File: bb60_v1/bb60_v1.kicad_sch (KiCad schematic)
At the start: 141 parts, among them J1 Conn_01x04, SW1 SW_Push, SW2 SW_Push, U1 STM32F072CBTx, U2 XC6206PxxxMR, U3 USBLC6-2SC6

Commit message: minor changes
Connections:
- net COL1: now also U1.12 (PA2); no longer U1.43 (PB7)
- net COL2: now also U1.11 (PA1); no longer U1.14 (PA4)
- net COL3: now also U1.10 (PA0); no longer U1.13 (PA3)
- net COL4: now also U1.43 (PB7); no longer U1.12 (PA2)
- net COL5: now also U1.14 (PA4); no longer U1.11 (PA1)
- net COL6: now also U1.13 (PA3); no longer U1.10 (PA0)
- net ROW2: now also U1.18 (PB0); no longer U1.16 (PA6)
- net ROW4: now also U1.16 (PA6); no longer U1.18 (PB0)
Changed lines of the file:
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@@
 	)
 	(label "ROW2"
-		(at 60.96 52.07 0)
-		(effects
-			(font
-				(size 1.27 1.27)
-			)
-			(justify left bottom)
+		(at 25.4 64.77 180)
+		(effects
+			(font
+				(size 1.27 1.27)
+			)
+			(justify right bottom)
 		)
 	)
 	(label "COL1"
-		(at 25.4 82.55 180)
-		(effects
-			(font
-				(size 1.27 1.27)
-			)
-			(justify right bottom)
+		(at 60.96 41.91 0)
+		(effects
+			(font
+				(size 1.27 1.27)
+			)
+			(justify left bottom)
 		)
 	)
@@
 	)
 	(label "COL6"
-		(at 60.96 36.83 0)
+		(at 60.96 44.45 0)
 		(effects
 			(font
@@
 	)
 	(label "COL2"
-		(at 60.96 46.99 0)
+		(at 60.96 39.37 0)
 		(effects
 			(font
@@
 	)
 	(label "COL3"
-		(at 60.96 44.45 0)
+		(at 60.96 36.83 0)
 		(effects
 			(font
@@
 	)
 	(label "COL5"
-		(at 60.96 39.37 0)
+		(at 60.96 46.99 0)
 		(effects
 			(font
@@
 	)
 	(label "COL4"
-		(at 60.96 41.91 0)
-		(effects
-			(font
-				(size 1.27 1.27)
-			)
-			(justify left bottom)
+		(at 25.4 82.55 180)
+		(effects
+			(font
+				(size 1.27 1.27)
+			)
+			(justify right bottom)
 		)
 	)
 	(label "ROW4"
-		(at 25.4 64.77 180)
-		(effects
-			(font
-				(size 1.27 1.27)
-			)
-			(justify right bottom)
-		)
-	)
+		(at 60.96 52.07 0)
+		(effects
+			(font
+				(size 1.27 1.27)
+			)
+			(justify left bottom)
+		)
+	)

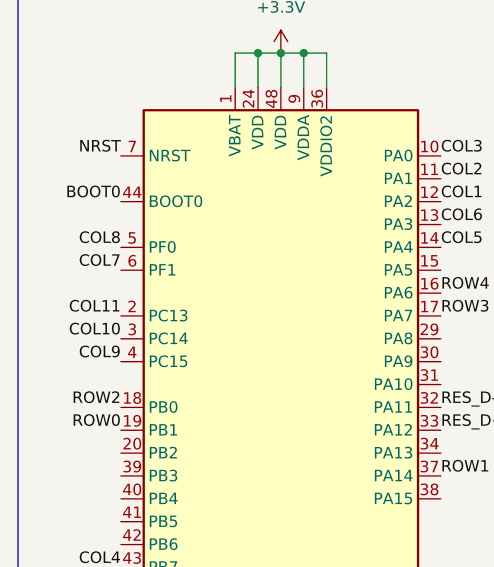
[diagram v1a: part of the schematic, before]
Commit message: Routed traces columns 7-11
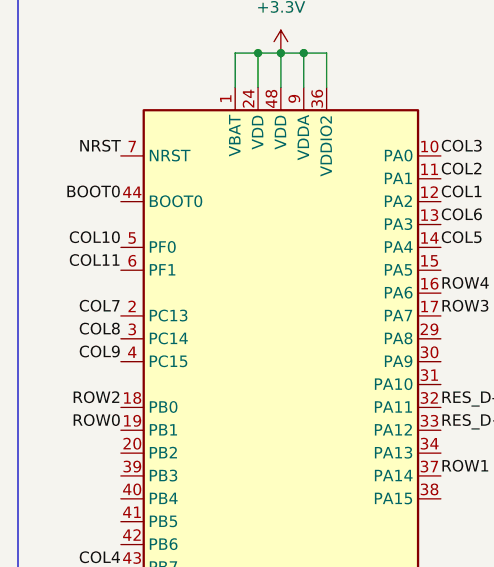
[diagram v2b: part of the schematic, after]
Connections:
- net COL10: now also U1.5 (PF0); no longer U1.3 (PC14)
- net COL11: now also U1.6 (PF1); no longer U1.2 (PC13)
- net COL7: now also U1.2 (PC13); no longer U1.6 (PF1)
- net COL8: now also U1.3 (PC14); no longer U1.5 (PF0)
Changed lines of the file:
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@@
 	)
 	(label "COL11"
-		(at 25.4 54.61 180)
+		(at 25.4 49.53 180)
 		(effects
 			(font
@@
 	)
 	(label "COL8"
-		(at 25.4 46.99 180)
+		(at 25.4 57.15 180)
 		(effects
 			(font
@@
 	)
 	(label "COL7"
-		(at 25.4 49.53 180)
+		(at 25.4 54.61 180)
 		(effects
 			(font
@@
 	)
 	(label "COL10"
-		(at 25.4 57.15 180)
+		(at 25.4 46.99 180)
 		(effects
 			(font

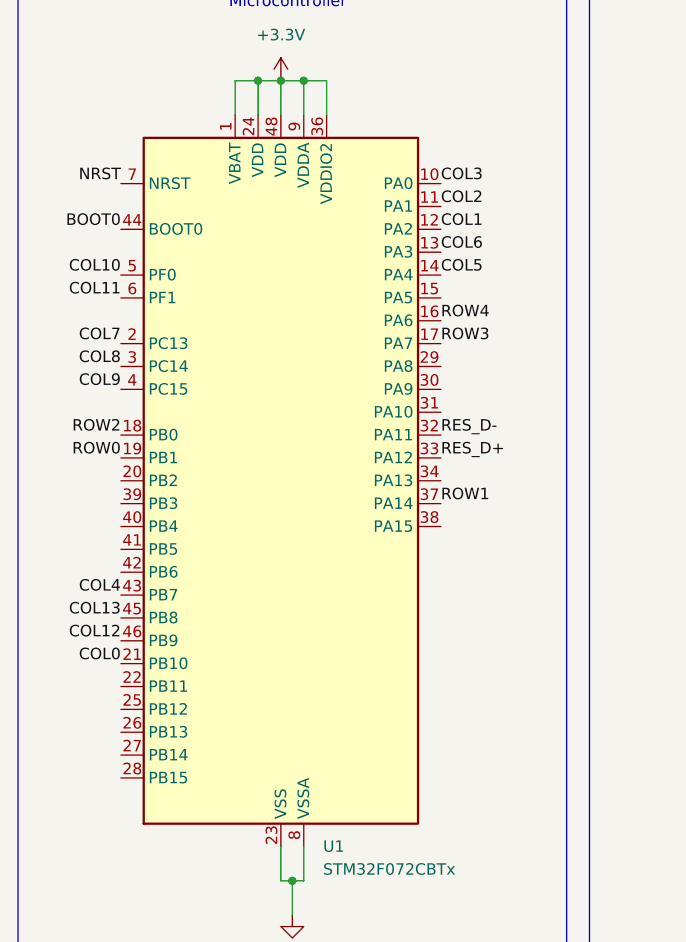
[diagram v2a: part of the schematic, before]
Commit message: finished row/column traces
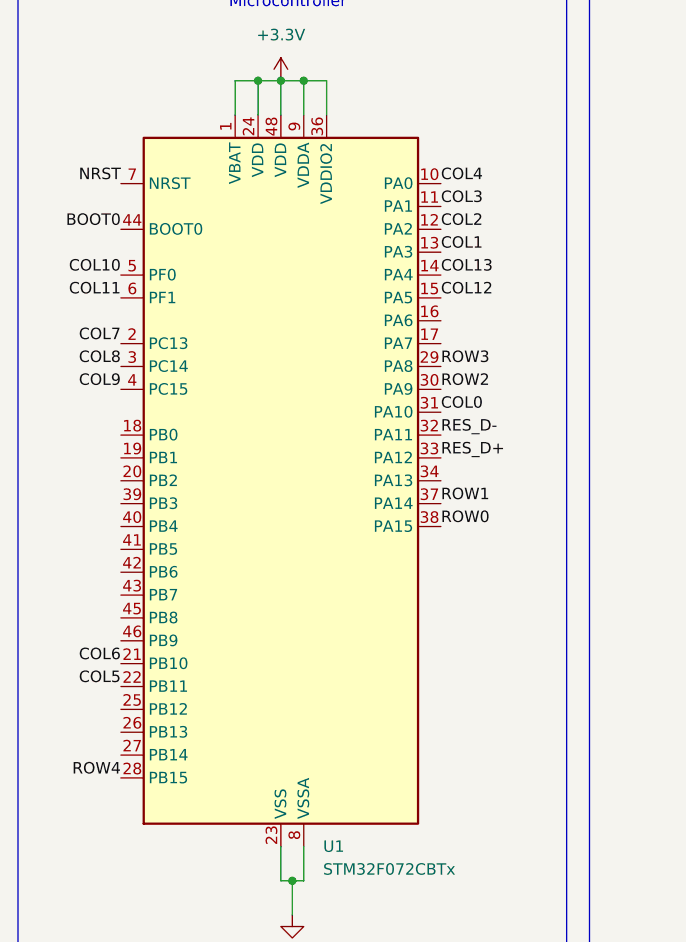
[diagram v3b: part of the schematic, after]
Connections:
- net COL0: now also U1.31 (PA10); no longer U1.21 (PB10)
- net COL1: now also U1.13 (PA3); no longer U1.12 (PA2)
- net COL12: now also U1.15 (PA5); no longer U1.46 (PB9)
- net COL13: now also U1.14 (PA4); no longer U1.45 (PB8)
- net COL2: now also U1.12 (PA2); no longer U1.11 (PA1)
- net COL3: now also U1.11 (PA1); no longer U1.10 (PA0)
- net COL4: now also U1.10 (PA0); no longer U1.43 (PB7)
- net COL5: now also U1.22 (PB11); no longer U1.14 (PA4)
- net COL6: now also U1.21 (PB10); no longer U1.13 (PA3)
- net ROW0: now also U1.38 (PA15); no longer U1.19 (PB1)
- net ROW2: now also U1.30 (PA9); no longer U1.18 (PB0)
- net ROW3: now also U1.29 (PA8); no longer U1.17 (PA7)
- net ROW4: now also U1.28 (PB15); no longer U1.16 (PA6)
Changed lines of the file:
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@@
 	)
 	(label "ROW2"
-		(at 25.4 64.77 180)
-		(effects
-			(font
-				(size 1.27 1.27)
-			)
-			(justify right bottom)
+		(at 60.96 59.69 0)
+		(effects
+			(font
+				(size 1.27 1.27)
+			)
+			(justify left bottom)
 		)
 	)
 	(label "COL1"
-		(at 60.96 41.91 0)
+		(at 60.96 44.45 0)
 		(effects
 			(font
@@
 	)
 	(label "COL0"
+		(at 60.96 62.23 0)
+		(effects
+			(font
+				(size 1.27 1.27)
+			)
+			(justify left bottom)
+		)
+	)
+	(label "COL13"
+		(at 60.96 46.99 0)
+		(effects
+			(font
+				(size 1.27 1.27)
+			)
+			(justify left bottom)
+		)
+	)
+	(label "COL6"
 		(at 25.4 90.17 180)
 		(effects
@@
 			)
 			(justify right bottom)
-		)
-	)
-	(label "COL13"
-		(at 25.4 85.09 180)
-		(effects
-			(font
-				(size 1.27 1.27)
-			)
-			(justify right bottom)
-		)
-	)
-	(label "COL6"
-		(at 60.96 44.45 0)
-		(effects
-			(font
-				(size 1.27 1.27)
-			)
-			(justify left bottom)
 		)
 	)
@@
 	)
 	(label "COL2"
+		(at 60.96 41.91 0)
+		(effects
+			(font
+				(size 1.27 1.27)
+			)
+			(justify left bottom)
+		)
+	)
+	(label "COL3"
 		(at 60.96 39.37 0)
-		(effects
-			(font
-				(size 1.27 1.27)
-			)
-			(justify left bottom)
-		)
-	)
-	(label "COL3"
-		(at 60.96 36.83 0)
 		(effects
 			(font
@@
 	)
 	(label "COL5"
-		(at 60.96 46.99 0)
-		(effects
-			(font
-				(size 1.27 1.27)
-			)
-			(justify left bottom)
+		(at 25.4 92.71 180)
+		(effects
+			(font
+				(size 1.27 1.27)
+			)
+			(justify right bottom)
 		)
 	)
@@
 	)
 	(label "COL12"
-		(at 25.4 87.63 180)
-		(effects
-			(font
-				(size 1.27 1.27)
-			)
-			(justify right bottom)
+		(at 60.96 49.53 0)
+		(effects
+			(font
+				(size 1.27 1.27)
+			)
+			(justify left bottom)
 		)
 	)
 	(label "ROW3"
-		(at 60.96 54.61 0)
+		(at 60.96 57.15 0)
 		(effects
 			(font
@@
 	)
 	(label "ROW0"
-		(at 25.4 67.31 180)
-		(effects
-			(font
-				(size 1.27 1.27)
-			)
-			(justify right bottom)
+		(at 60.96 74.93 0)
+		(effects
+			(font
+				(size 1.27 1.27)
+			)
+			(justify left bottom)
 		)
 	)
 	(label "COL4"
-		(at 25.4 82.55 180)
-		(effects
-			(font
-				(size 1.27 1.27)
-			)
-			(justify right bottom)
+		(at 60.96 36.83 0)
+		(effects
+			(font
+				(size 1.27 1.27)
+			)
+			(justify left bottom)
 		)
 	)
 	(label "ROW4"
-		(at 60.96 52.07 0)
-		(effects
-			(font
-				(size 1.27 1.27)
-			)
-			(justify left bottom)
-		)
-	)
+		(at 25.4 102.87 180)
+		(effects
+			(font
+				(size 1.27 1.27)
+			)
+			(justify right bottom)
+		)
+	)

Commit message: Rerouted everything
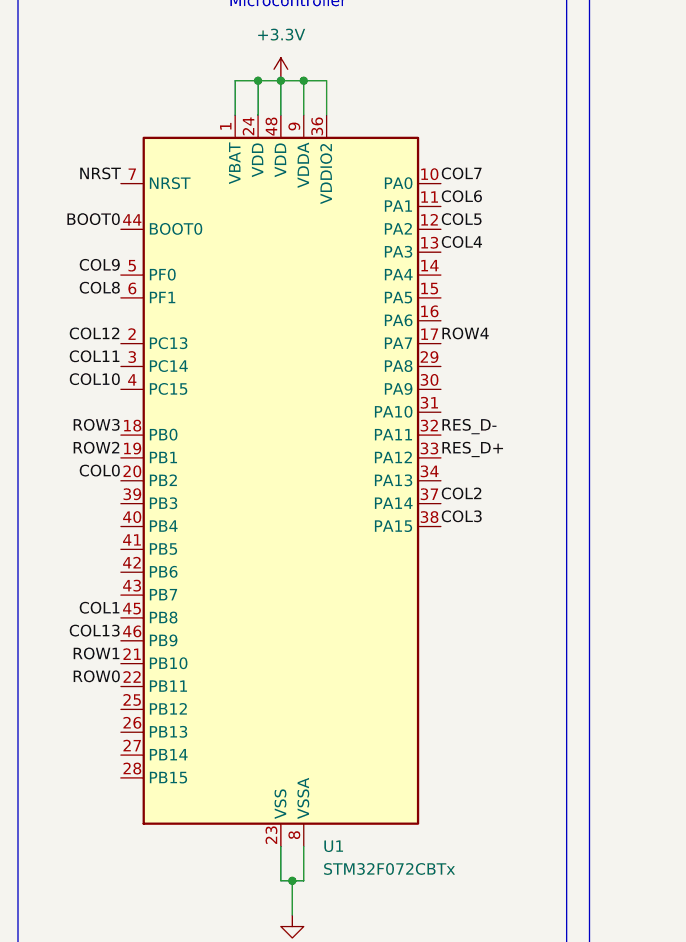
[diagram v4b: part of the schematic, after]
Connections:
- net COL0: now also U1.20 (PB2); no longer U1.31 (PA10)
- net COL1: now also U1.45 (PB8); no longer U1.13 (PA3)
- net COL10: now also U1.4 (PC15); no longer U1.5 (PF0)
- net COL11: now also U1.3 (PC14); no longer U1.6 (PF1)
- net COL12: now also U1.2 (PC13); no longer U1.15 (PA5)
- net COL13: now also U1.46 (PB9); no longer U1.14 (PA4)
- net COL2: now also U1.37 (PA14); no longer U1.12 (PA2)
- net COL3: now also U1.38 (PA15); no longer U1.11 (PA1)
- net COL4: now also U1.13 (PA3); no longer U1.10 (PA0)
- net COL5: now also U1.12 (PA2); no longer U1.22 (PB11)
- net COL6: now also U1.11 (PA1); no longer U1.21 (PB10)
- net COL7: now also U1.10 (PA0); no longer U1.2 (PC13)
- net COL8: now also U1.6 (PF1); no longer U1.3 (PC14)
- net COL9: now also U1.5 (PF0); no longer U1.4 (PC15)
- net ROW0: now also U1.22 (PB11); no longer U1.38 (PA15)
- net ROW1: now also U1.21 (PB10); no longer U1.37 (PA14)
- net ROW2: now also U1.19 (PB1); no longer U1.30 (PA9)
- net ROW3: now also U1.18 (PB0); no longer U1.29 (PA8)
- net ROW4: now also U1.17 (PA7); no longer U1.28 (PB15)
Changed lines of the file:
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@@
 	)
 	(label "COL11"
-		(at 25.4 49.53 180)
+		(at 25.4 57.15 180)
 		(effects
 			(font
@@
 	)
 	(label "ROW2"
-		(at 60.96 59.69 0)
-		(effects
-			(font
-				(size 1.27 1.27)
-			)
-			(justify left bottom)
+		(at 25.4 67.31 180)
+		(effects
+			(font
+				(size 1.27 1.27)
+			)
+			(justify right bottom)
 		)
 	)
 	(label "COL1"
-		(at 60.96 44.45 0)
-		(effects
-			(font
-				(size 1.27 1.27)
-			)
-			(justify left bottom)
+		(at 25.4 85.09 180)
+		(effects
+			(font
+				(size 1.27 1.27)
+			)
+			(justify right bottom)
 		)
 	)
@@
 	)
 	(label "COL0"
-		(at 60.96 62.23 0)
-		(effects
-			(font
-				(size 1.27 1.27)
-			)
-			(justify left bottom)
+		(at 25.4 69.85 180)
+		(effects
+			(font
+				(size 1.27 1.27)
+			)
+			(justify right bottom)
 		)
 	)
 	(label "COL13"
-		(at 60.96 46.99 0)
-		(effects
-			(font
-				(size 1.27 1.27)
-			)
-			(justify left bottom)
+		(at 25.4 87.63 180)
+		(effects
+			(font
+				(size 1.27 1.27)
+			)
+			(justify right bottom)
 		)
 	)
 	(label "COL6"
-		(at 25.4 90.17 180)
-		(effects
-			(font
-				(size 1.27 1.27)
-			)
-			(justify right bottom)
+		(at 60.96 39.37 0)
+		(effects
+			(font
+				(size 1.27 1.27)
+			)
+			(justify left bottom)
 		)
 	)
@@
 	)
 	(label "ROW1"
-		(at 60.96 72.39 0)
-		(effects
-			(font
-				(size 1.27 1.27)
-			)
-			(justify left bottom)
+		(at 25.4 90.17 180)
+		(effects
+			(font
+				(size 1.27 1.27)
+			)
+			(justify right bottom)
 		)
 	)
 	(label "COL8"
-		(at 25.4 57.15 180)
+		(at 25.4 49.53 180)
 		(effects
 			(font
@@
 	)
 	(label "COL7"
-		(at 25.4 54.61 180)
-		(effects
-			(font
-				(size 1.27 1.27)
-			)
-			(justify right bottom)
+		(at 60.96 36.83 0)
+		(effects
+			(font
+				(size 1.27 1.27)
+			)
+			(justify left bottom)
 		)
 	)
@@
 	)
 	(label "COL10"
-		(at 25.4 46.99 180)
+		(at 25.4 59.69 180)
 		(effects
 			(font
@@
 	)
 	(label "COL2"
-		(at 60.96 41.91 0)
+		(at 60.96 72.39 0)
 		(effects
 			(font
@@
 	)
 	(label "COL3"
-		(at 60.96 39.37 0)
+		(at 60.96 74.93 0)
 		(effects
 			(font
@@
 	)
 	(label "COL5"
-		(at 25.4 92.71 180)
-		(effects
-			(font
-				(size 1.27 1.27)
-			)
-			(justify right bottom)
+		(at 60.96 41.91 0)
+		(effects
+			(font
+				(size 1.27 1.27)
+			)
+			(justify left bottom)
 		)
 	)
@@
 	)
 	(label "COL9"
-		(at 25.4 59.69 180)
+		(at 25.4 46.99 180)
 		(effects
 			(font
@@
 	)
 	(label "COL12"
-		(at 60.96 49.53 0)
-		(effects
-			(font
-				(size 1.27 1.27)
-			)
-			(justify left bottom)
+		(at 25.4 54.61 180)
+		(effects
+			(font
+				(size 1.27 1.27)
+			)
+			(justify right bottom)
 		)
 	)
 	(label "ROW3"
-		(at 60.96 57.15 0)
-		(effects
-			(font
-				(size 1.27 1.27)
-			)
-			(justify left bottom)
+		(at 25.4 64.77 180)
+		(effects
+			(font
+				(size 1.27 1.27)
+			)
+			(justify right bottom)
 		)
 	)
 	(label "ROW0"
-		(at 60.96 74.93 0)
-		(effects
-			(font
-				(size 1.27 1.27)
-			)
-			(justify left bottom)
+		(at 25.4 92.71 180)
+		(effects
+			(font
+				(size 1.27 1.27)
+			)
+			(justify right bottom)
 		)
 	)
 	(label "COL4"
-		(at 60.96 36.83 0)
+		(at 60.96 44.45 0)
 		(effects
 			(font
@@
 	)
 	(label "ROW4"
-		(at 25.4 102.87 180)
-		(effects
-			(font
-				(size 1.27 1.27)
-			)
-			(justify right bottom)
-		)
-	)
+		(at 60.96 54.61 0)
+		(effects
+			(font
+				(size 1.27 1.27)
+			)
+			(justify left bottom)
+		)
+	)

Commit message: idk what i changed here
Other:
- note removed: "to fix: check regulator pin continuity"
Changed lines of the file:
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@@
-		)
-	)
-	(text "to fix: check regulator pin continuity"
-		(exclude_from_sim no)
-		(at 86.614 189.484 0)
-		(effects
-			(font
-				(size 1.27 1.27)
-			)
 		)
 	)

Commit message: Final changes
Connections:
- net COL2: now also U1.38 (PA15); no longer U1.37 (PA14)
- net COL3: now also U1.39 (PB3); no longer U1.38 (PA15)
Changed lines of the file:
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@@
 	)
 	(label "COL2"
-		(at 60.96 72.39 0)
+		(at 60.96 74.93 0)
 		(effects
 			(font
@@
 	)
 	(label "COL3"
-		(at 60.96 74.93 0)
+		(at 25.4 72.39 180)
 		(effects
 			(font
 				(size 1.27 1.27)
 			)
-			(justify left bottom)
+			(justify right bottom)
 		)
 	)
